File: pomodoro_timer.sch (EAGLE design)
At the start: 17 parts

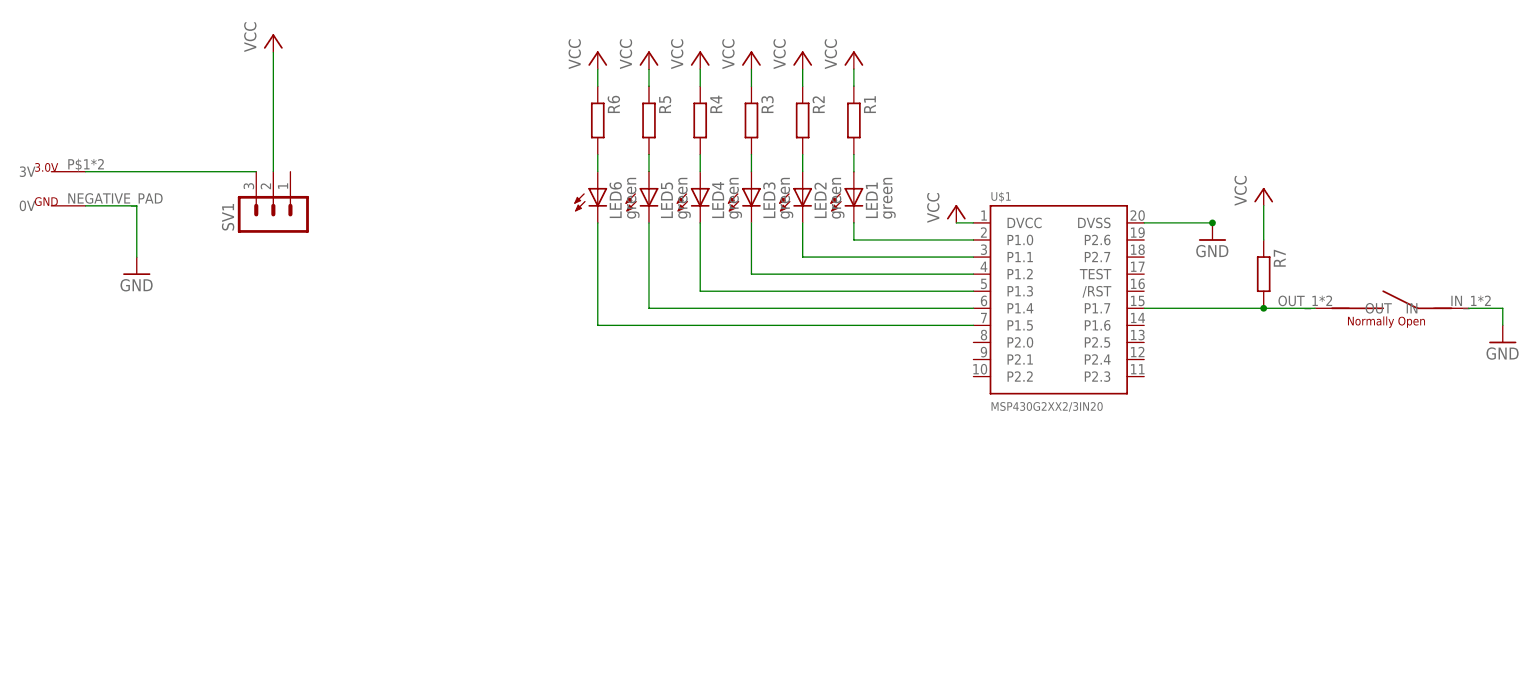
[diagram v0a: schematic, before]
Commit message: added ground plane + jumper for test input
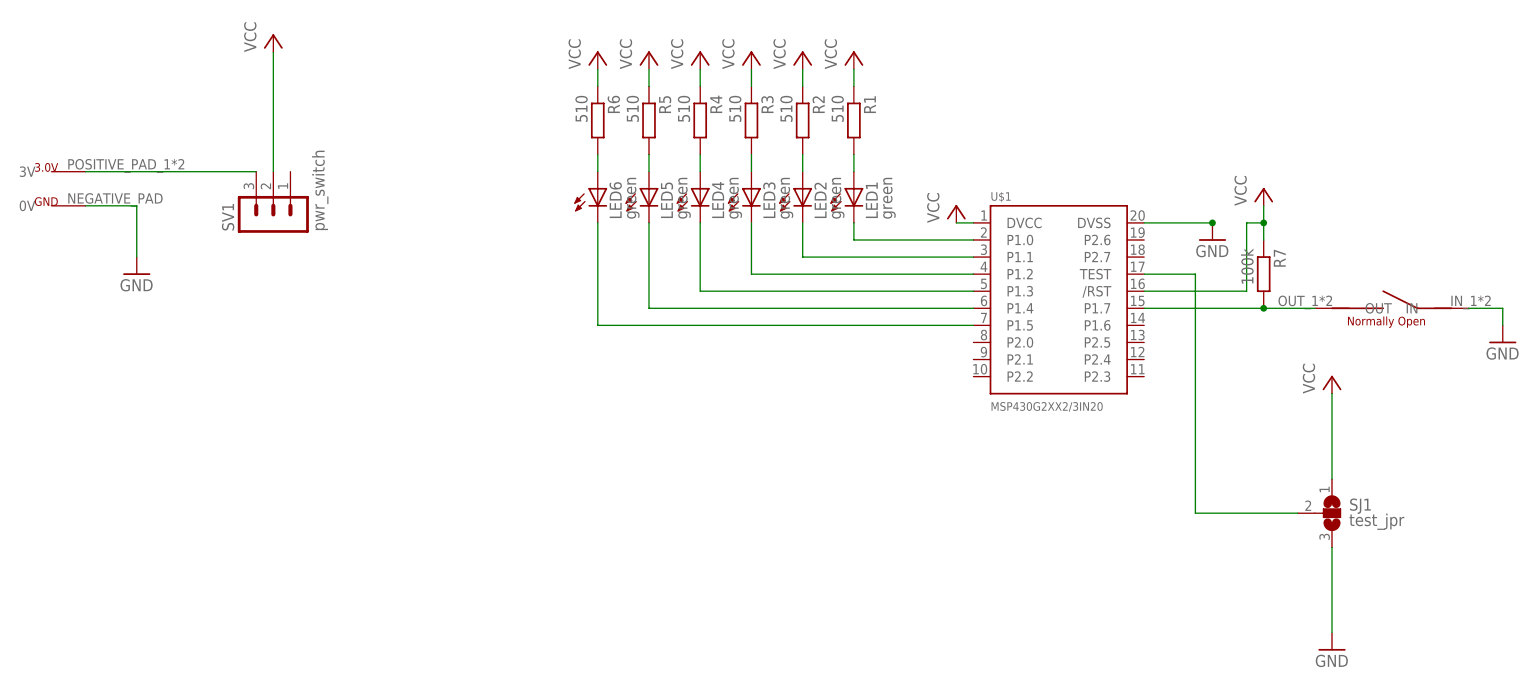
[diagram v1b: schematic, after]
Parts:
- added SJ1: test_jpr, jumper:SJ2W
- R1, R2, R3, R4, R5, R6: value (none) -> 510
- R7: value (none) -> 100k
- SV1: value (none) -> pwr_switch
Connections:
- net N$1 renamed POS_BAT
- new net N$15: SJ1.2, U$1.TEST
- net GND: now also SJ1.3
- net VCC: now also SJ1.1, U$1./RST
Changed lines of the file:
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@@
 <part name="GND1" library="supply1" deviceset="GND" device=""/>
 <part name="GND2" library="supply1" deviceset="GND" device=""/>
-<part name="R1" library="resistor" deviceset="R-EU_" device="M1206"/>
-<part name="R2" library="resistor" deviceset="R-EU_" device="M1206"/>
-<part name="R3" library="resistor" deviceset="R-EU_" device="M1206"/>
-<part name="R4" library="resistor" deviceset="R-EU_" device="M1206"/>
-<part name="R5" library="resistor" deviceset="R-EU_" device="M1206"/>
-<part name="R6" library="resistor" deviceset="R-EU_" device="M1206"/>
+<part name="R1" library="resistor" deviceset="R-EU_" device="M1206" value="510"/>
+<part name="R2" library="resistor" deviceset="R-EU_" device="M1206" value="510"/>
+<part name="R3" library="resistor" deviceset="R-EU_" device="M1206" value="510"/>
+<part name="R4" library="resistor" deviceset="R-EU_" device="M1206" value="510"/>
+<part name="R5" library="resistor" deviceset="R-EU_" device="M1206" value="510"/>
+<part name="R6" library="resistor" deviceset="R-EU_" device="M1206" value="510"/>
 <part name="P+1" library="supply1" deviceset="VCC" device=""/>
 <part name="P+2" library="supply1" deviceset="VCC" device=""/>
@@
 <part name="P+7" library="supply1" deviceset="VCC" device=""/>
 <part name="P+8" library="supply1" deviceset="VCC" device=""/>
-<part name="R7" library="resistor" deviceset="R-EU_" device="M1206"/>
+<part name="R7" library="resistor" deviceset="R-EU_" device="M1206" value="100k"/>
 <part name="P+9" library="supply1" deviceset="VCC" device=""/>
-<part name="U$2" library="CR2032_HOLDER" deviceset="CR2032_HOLDER" device="NORMAL"/>
 <part name="U$3" library="SWITCH_SIMPLE" deviceset="SWITCH_SIMPLE" device="NORMAL"/>
 <part name="GND3" library="supply1" deviceset="GND" device=""/>
-<part name="SV1" library="con-lstb" deviceset="MA03-1" device=""/>
+<part name="SV1" library="con-lstb" deviceset="MA03-1" device="" value="pwr_switch"/>
+<part name="GND4" library="supply1" deviceset="GND" device=""/>
+<part name="P+10" library="supply1" deviceset="VCC" device=""/>
+<part name="SJ1" library="jumper" deviceset="SJ2W" device="" value="test_jpr"/>
+<part name="U$2" library="CR2032_HOLDER" deviceset="CR2032_HOLDER" device="NORMAL"/>
 </parts>
 <sheets>
@@
 <instance part="R7" gate="G$1" x="27.94" y="96.52" rot="R270"/>
 <instance part="P+9" gate="VCC" x="27.94" y="109.22"/>
-<instance part="U$2" gate="G$1" x="-152.4" y="109.22"/>
 <instance part="U$3" gate="G$1" x="45.72" y="91.44" rot="MR0"/>
 <instance part="GND3" gate="1" x="63.5" y="86.36"/>
 <instance part="SV1" gate="G$1" x="-119.38" y="104.14" rot="R90"/>
+<instance part="GND4" gate="1" x="38.1" y="40.64"/>
+<instance part="P+10" gate="VCC" x="38.1" y="81.28"/>
+<instance part="SJ1" gate="G$1" x="38.1" y="60.96"/>
+<instance part="U$2" gate="G$1" x="-152.4" y="109.22"/>
 </instances>
 <busses>
@@
 </segment>
 <segment>
-<pinref part="U$2" gate="G$1" pin="0V"/>
 <pinref part="GND2" gate="1" pin="GND"/>
 <wire x1="-147.32" y1="106.68" x2="-139.7" y2="106.68" width="0.1524" layer="91"/>
 <wire x1="-139.7" y1="106.68" x2="-139.7" y2="99.06" width="0.1524" layer="91"/>
+<pinref part="U$2" gate="G$1" pin="0V"/>
 </segment>
 <segment>
@@
 <pinref part="GND3" gate="1" pin="GND"/>
 </segment>
+<segment>
+<pinref part="SJ1" gate="G$1" pin="3"/>
+<pinref part="GND4" gate="1" pin="GND"/>
+<wire x1="38.1" y1="55.88" x2="38.1" y2="43.18" width="0.1524" layer="91"/>
+</segment>
 </net>
 <net name="N$3" class="0">
@@
 <pinref part="R7" gate="G$1" pin="1"/>
 <pinref part="P+9" gate="VCC" pin="VCC"/>
-<wire x1="27.94" y1="106.68" x2="27.94" y2="101.6" width="0.1524" layer="91"/>
+<wire x1="27.94" y1="106.68" x2="27.94" y2="104.14" width="0.1524" layer="91"/>
+<pinref part="U$1" gate="G$1" pin="/RST"/>
+<wire x1="27.94" y1="104.14" x2="27.94" y2="101.6" width="0.1524" layer="91"/>
+<wire x1="10.16" y1="93.98" x2="25.4" y2="93.98" width="0.1524" layer="91"/>
+<wire x1="25.4" y1="93.98" x2="25.4" y2="104.14" width="0.1524" layer="91"/>
+<wire x1="25.4" y1="104.14" x2="27.94" y2="104.14" width="0.1524" layer="91"/>
+<junction x="27.94" y="104.14"/>
 </segment>
 <segment>
@@
 <pinref part="SV1" gate="G$1" pin="2"/>
 <wire x1="-119.38" y1="129.54" x2="-119.38" y2="111.76" width="0.1524" layer="91"/>
+</segment>
+<segment>
+<pinref part="P+10" gate="VCC" pin="VCC"/>
+<pinref part="SJ1" gate="G$1" pin="1"/>
+<wire x1="38.1" y1="78.74" x2="38.1" y2="66.04" width="0.1524" layer="91"/>
 </segment>
 </net>
@@
 </segment>
 </net>
-<net name="N$1" class="0">
-<segment>
-<pinref part="U$2" gate="G$1" pin="3V"/>
+<net name="POS_BAT" class="0">
+<segment>
 <pinref part="SV1" gate="G$1" pin="3"/>
 <wire x1="-147.32" y1="111.76" x2="-121.92" y2="111.76" width="0.1524" layer="91"/>
+<pinref part="U$2" gate="G$1" pin="3V"/>
 </segment>
 </net>
@@
 </segment>
 </net>
+<net name="N$15" class="0">
+<segment>
+<wire x1="17.78" y1="60.96" x2="17.78" y2="96.52" width="0.1524" layer="91"/>
+<pinref part="U$1" gate="G$1" pin="TEST"/>
+<wire x1="17.78" y1="96.52" x2="10.16" y2="96.52" width="0.1524" layer="91"/>
+<pinref part="SJ1" gate="G$1" pin="2"/>
+<wire x1="17.78" y1="60.96" x2="33.02" y2="60.96" width="0.1524" layer="91"/>
+</segment>
+</net>
